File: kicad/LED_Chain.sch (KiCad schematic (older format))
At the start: 30 parts, among them J1 Interface, J2 PWR, J3 NeoPixel R1 A, J4 NeoPixel R1 B, J5 NeoPixel R1 C, J6 NeoPixel R1 D, J7 LED, Q1 IRLML2502, Q2 IRLML2502, Q3 IRLML2502, Q4 IRLML2502, U1 HCF4027B, U2 74LS04

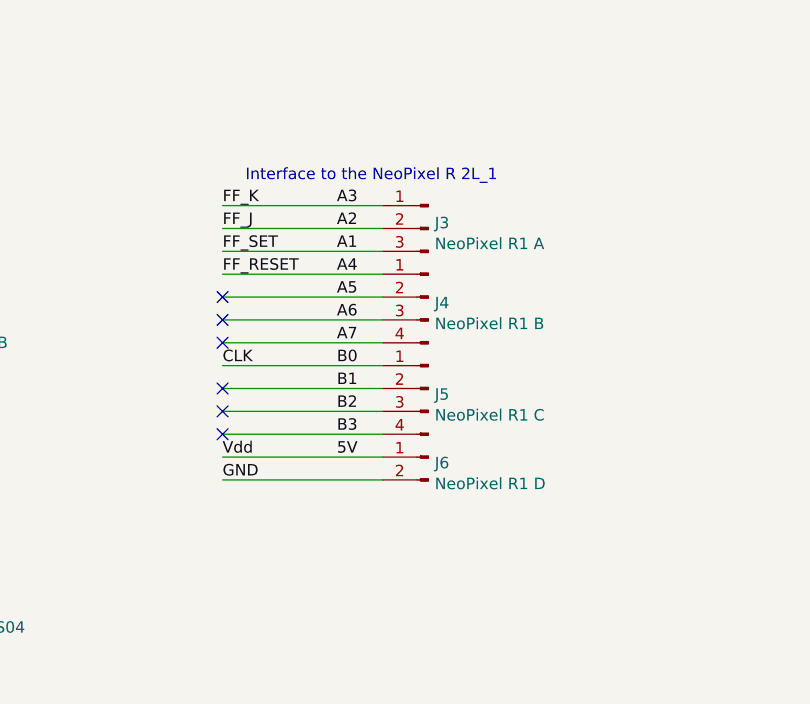
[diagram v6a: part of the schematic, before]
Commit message: Fixes the pin association on J3
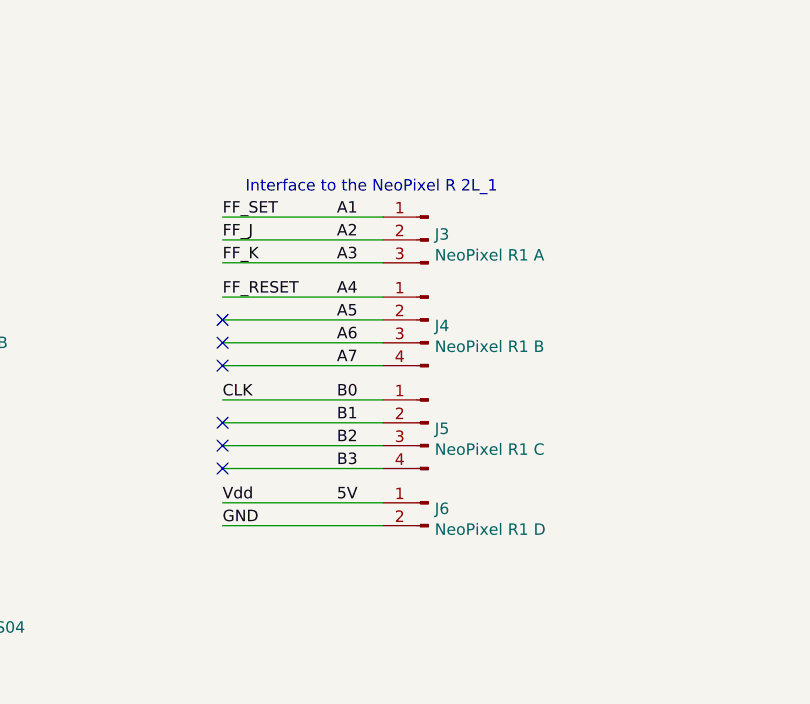
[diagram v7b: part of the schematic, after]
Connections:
- net A1: now also J3.1 (Pin_1); no longer J3.3 (Pin_3)
- net A3: now also J3.3 (Pin_3); no longer J3.1 (Pin_1)
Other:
- moved on the sheet: J3, J4, J5, J6
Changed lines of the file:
@@
 L Connector:Conn_01x04_Male J5
 U 1 1 5FA85238
-P 7750 5050
-F 0 "J5" H 7722 5024 50  0000 R CNN
-F 1 "NeoPixel R1 C" H 7722 4933 50  0000 R CNN
-F 2 "Pin_Headers:Pin_Header_Straight_1x04_Pitch2.54mm" H 7750 5050 50  0001 C CNN
-F 3 "~" H 7750 5050 50  0001 C CNN
-	1    7750 5050
+P 7750 5200
+F 0 "J5" H 7722 5174 50  0000 R CNN
+F 1 "NeoPixel R1 C" H 7722 5083 50  0000 R CNN
+F 2 "Pin_Headers:Pin_Header_Straight_1x04_Pitch2.54mm" H 7750 5200 50  0001 C CNN
+F 3 "~" H 7750 5200 50  0001 C CNN
+	1    7750 5200
 	-1   0    0    -1
 $EndComp
@@
 L Connector:Conn_01x04_Male J4
 U 1 1 5FA870C1
-P 7750 4650
-F 0 "J4" H 7722 4624 50  0000 R CNN
-F 1 "NeoPixel R1 B" H 7722 4533 50  0000 R CNN
-F 2 "Pin_Headers:Pin_Header_Straight_1x04_Pitch2.54mm" H 7750 4650 50  0001 C CNN
-F 3 "~" H 7750 4650 50  0001 C CNN
-	1    7750 4650
+P 7750 4750
+F 0 "J4" H 7722 4724 50  0000 R CNN
+F 1 "NeoPixel R1 B" H 7722 4633 50  0000 R CNN
+F 2 "Pin_Headers:Pin_Header_Straight_1x04_Pitch2.54mm" H 7750 4750 50  0001 C CNN
+F 3 "~" H 7750 4750 50  0001 C CNN
+	1    7750 4750
 	-1   0    0    -1
 $EndComp
@@
 L Connector:Conn_01x03_Male J3
 U 1 1 5FA916E0
-P 7750 4350
-F 0 "J3" H 7722 4374 50  0000 R CNN
-F 1 "NeoPixel R1 A" H 7722 4283 50  0000 R CNN
-F 2 "Pin_Headers:Pin_Header_Straight_1x03_Pitch2.54mm" H 7750 4350 50  0001 C CNN
-F 3 "~" H 7750 4350 50  0001 C CNN
-	1    7750 4350
+P 7750 4400
+F 0 "J3" H 7722 4424 50  0000 R CNN
+F 1 "NeoPixel R1 A" H 7722 4333 50  0000 R CNN
+F 2 "Pin_Headers:Pin_Header_Straight_1x03_Pitch2.54mm" H 7750 4400 50  0001 C CNN
+F 3 "~" H 7750 4400 50  0001 C CNN
+	1    7750 4400
 	-1   0    0    -1
 $EndComp
-Wire Wire Line
-	7550 4550 6850 4550
 Wire Wire Line
 	7550 4650 6850 4650
@@
 	7550 4950 6850 4950
 Wire Wire Line
-	7550 5050 6850 5050
+	7550 5100 6850 5100
 Wire Wire Line
-	7550 5250 6850 5250
+	7550 5200 6850 5200
 Wire Wire Line
-	7550 4250 6850 4250
+	7550 5400 6850 5400
 Wire Wire Line
-	7550 4350 6850 4350
+	7550 4300 6850 4300
 Wire Wire Line
-	7550 4450 6850 4450
-Text Label 7350 4550 0    50   ~ 0
+	7550 4400 6850 4400
+Wire Wire Line
+	7550 4500 6850 4500
+Text Label 7350 4650 0    50   ~ 0
 A4
-Text Label 7350 4650 0    50   ~ 0
+Text Label 7350 4750 0    50   ~ 0
 A5
-Text Label 7350 4750 0    50   ~ 0
+Text Label 7350 4850 0    50   ~ 0
 A6
-Text Label 7350 4850 0    50   ~ 0
+Text Label 7350 4950 0    50   ~ 0
 A7
-Text Label 7350 5250 0    50   ~ 0
+Text Label 7350 5400 0    50   ~ 0
 B3
-Text Label 7350 5150 0    50   ~ 0
+Text Label 7350 5300 0    50   ~ 0
 B2
-Text Label 7350 5050 0    50   ~ 0
+Text Label 7350 5200 0    50   ~ 0
 B1
-Text Label 7350 4950 0    50   ~ 0
+Text Label 7350 5100 0    50   ~ 0
 B0
-Text Label 7350 4250 0    50   ~ 0
+Text Label 7350 4500 0    50   ~ 0
 A3
-Text Label 7350 4350 0    50   ~ 0
+Text Label 7350 4400 0    50   ~ 0
 A2
-Text Label 7350 4450 0    50   ~ 0
+Text Label 7350 4300 0    50   ~ 0
 A1
 Wire Wire Line
@@
 	3450 5650 3200 5650
 Wire Wire Line
-	7550 5350 6850 5350
+	7550 5550 6850 5550
 Wire Wire Line
-	7550 5450 6850 5450
-Text Label 7350 5350 0    50   ~ 0
+	7550 5650 6850 5650
+Text Label 7350 5550 0    50   ~ 0
 5V
-Text Label 6850 5450 0    50   ~ 0
+Text Label 6850 5650 0    50   ~ 0
 GND
 $Comp
 L Connector:Conn_01x02_Male J6
 U 1 1 5FAE3734
-P 7750 5350
-F 0 "J6" H 7722 5324 50  0000 R CNN
-F 1 "NeoPixel R1 D" H 7722 5233 50  0000 R CNN
-F 2 "Pin_Headers:Pin_Header_Straight_1x02_Pitch2.54mm" H 7750 5350 50  0001 C CNN
-F 3 "~" H 7750 5350 50  0001 C CNN
-	1    7750 5350
+P 7750 5550
+F 0 "J6" H 7722 5524 50  0000 R CNN
+F 1 "NeoPixel R1 D" H 7722 5433 50  0000 R CNN
+F 2 "Pin_Headers:Pin_Header_Straight_1x02_Pitch2.54mm" H 7750 5550 50  0001 C CNN
+F 3 "~" H 7750 5550 50  0001 C CNN
+	1    7750 5550
 	-1   0    0    -1
 $EndComp
@@
 	-1   0    0    -1
 $EndComp
-Text Notes 6950 4150 0    50   ~ 0
+Text Notes 6950 4200 0    50   ~ 0
 Interface to the NeoPixel R 2L_1
 Text Notes 2900 5850 0    50   ~ 0
 Jumper for common Vbb and Vdd
 Wire Wire Line
-	7550 5150 6850 5150
-Text Label 6850 4950 0    50   ~ 0
+	7550 5300 6850 5300
+Text Label 6850 5100 0    50   ~ 0
 CLK
-Text Label 6850 4350 0    50   ~ 0
+Text Label 6850 4400 0    50   ~ 0
 FF_J
-Text Label 6850 4250 0    50   ~ 0
+Text Label 6850 4500 0    50   ~ 0
 FF_K
-Text Label 6850 4450 0    50   ~ 0
+Text Label 6850 4300 0    50   ~ 0
 FF_SET
-Text Label 6850 4550 0    50   ~ 0
+Text Label 6850 4650 0    50   ~ 0
 FF_RESET
-Text Label 6850 5350 0    50   ~ 0
+Text Label 6850 5550 0    50   ~ 0
 Vdd
-NoConn ~ 6850 4650
 NoConn ~ 6850 4750
 NoConn ~ 6850 4850
-NoConn ~ 6850 5250
-NoConn ~ 6850 5050
-NoConn ~ 6850 5150
+NoConn ~ 6850 4950
+NoConn ~ 6850 5400
+NoConn ~ 6850 5200
+NoConn ~ 6850 5300
 Wire Wire Line
 	2750 4450 3000 4450

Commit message: Revert "Fixes the pin association on J3"
This reverts commit 2cc36517f423e818af2cf15adf9433c164440afc.
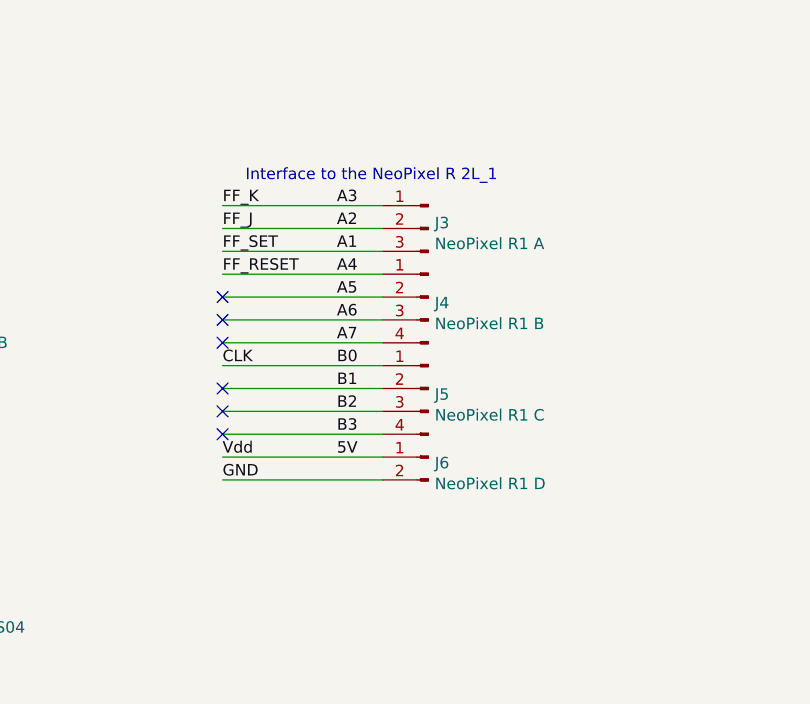
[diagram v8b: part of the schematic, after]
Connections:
- net A1: now also J3.3 (Pin_3); no longer J3.1 (Pin_1)
- net A3: now also J3.1 (Pin_1); no longer J3.3 (Pin_3)
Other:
- moved on the sheet: J3, J4, J5, J6
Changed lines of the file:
@@
 L Connector:Conn_01x04_Male J5
 U 1 1 5FA85238
-P 7750 5200
-F 0 "J5" H 7722 5174 50  0000 R CNN
-F 1 "NeoPixel R1 C" H 7722 5083 50  0000 R CNN
-F 2 "Pin_Headers:Pin_Header_Straight_1x04_Pitch2.54mm" H 7750 5200 50  0001 C CNN
-F 3 "~" H 7750 5200 50  0001 C CNN
-	1    7750 5200
+P 7750 5050
+F 0 "J5" H 7722 5024 50  0000 R CNN
+F 1 "NeoPixel R1 C" H 7722 4933 50  0000 R CNN
+F 2 "Pin_Headers:Pin_Header_Straight_1x04_Pitch2.54mm" H 7750 5050 50  0001 C CNN
+F 3 "~" H 7750 5050 50  0001 C CNN
+	1    7750 5050
 	-1   0    0    -1
 $EndComp
@@
 L Connector:Conn_01x04_Male J4
 U 1 1 5FA870C1
-P 7750 4750
-F 0 "J4" H 7722 4724 50  0000 R CNN
-F 1 "NeoPixel R1 B" H 7722 4633 50  0000 R CNN
-F 2 "Pin_Headers:Pin_Header_Straight_1x04_Pitch2.54mm" H 7750 4750 50  0001 C CNN
-F 3 "~" H 7750 4750 50  0001 C CNN
-	1    7750 4750
+P 7750 4650
+F 0 "J4" H 7722 4624 50  0000 R CNN
+F 1 "NeoPixel R1 B" H 7722 4533 50  0000 R CNN
+F 2 "Pin_Headers:Pin_Header_Straight_1x04_Pitch2.54mm" H 7750 4650 50  0001 C CNN
+F 3 "~" H 7750 4650 50  0001 C CNN
+	1    7750 4650
 	-1   0    0    -1
 $EndComp
@@
 L Connector:Conn_01x03_Male J3
 U 1 1 5FA916E0
-P 7750 4400
-F 0 "J3" H 7722 4424 50  0000 R CNN
-F 1 "NeoPixel R1 A" H 7722 4333 50  0000 R CNN
-F 2 "Pin_Headers:Pin_Header_Straight_1x03_Pitch2.54mm" H 7750 4400 50  0001 C CNN
-F 3 "~" H 7750 4400 50  0001 C CNN
-	1    7750 4400
+P 7750 4350
+F 0 "J3" H 7722 4374 50  0000 R CNN
+F 1 "NeoPixel R1 A" H 7722 4283 50  0000 R CNN
+F 2 "Pin_Headers:Pin_Header_Straight_1x03_Pitch2.54mm" H 7750 4350 50  0001 C CNN
+F 3 "~" H 7750 4350 50  0001 C CNN
+	1    7750 4350
 	-1   0    0    -1
 $EndComp
+Wire Wire Line
+	7550 4550 6850 4550
 Wire Wire Line
 	7550 4650 6850 4650
@@
 	7550 4950 6850 4950
 Wire Wire Line
-	7550 5100 6850 5100
+	7550 5050 6850 5050
 Wire Wire Line
-	7550 5200 6850 5200
+	7550 5250 6850 5250
 Wire Wire Line
-	7550 5400 6850 5400
+	7550 4250 6850 4250
 Wire Wire Line
-	7550 4300 6850 4300
+	7550 4350 6850 4350
 Wire Wire Line
-	7550 4400 6850 4400
-Wire Wire Line
-	7550 4500 6850 4500
+	7550 4450 6850 4450
+Text Label 7350 4550 0    50   ~ 0
+A4
 Text Label 7350 4650 0    50   ~ 0
-A4
+A5
 Text Label 7350 4750 0    50   ~ 0
-A5
+A6
 Text Label 7350 4850 0    50   ~ 0
-A6
+A7
+Text Label 7350 5250 0    50   ~ 0
+B3
+Text Label 7350 5150 0    50   ~ 0
+B2
+Text Label 7350 5050 0    50   ~ 0
+B1
 Text Label 7350 4950 0    50   ~ 0
-A7
-Text Label 7350 5400 0    50   ~ 0
-B3
-Text Label 7350 5300 0    50   ~ 0
-B2
-Text Label 7350 5200 0    50   ~ 0
-B1
-Text Label 7350 5100 0    50   ~ 0
 B0
-Text Label 7350 4500 0    50   ~ 0
+Text Label 7350 4250 0    50   ~ 0
 A3
-Text Label 7350 4400 0    50   ~ 0
+Text Label 7350 4350 0    50   ~ 0
 A2
-Text Label 7350 4300 0    50   ~ 0
+Text Label 7350 4450 0    50   ~ 0
 A1
 Wire Wire Line
@@
 	3450 5650 3200 5650
 Wire Wire Line
-	7550 5550 6850 5550
+	7550 5350 6850 5350
 Wire Wire Line
-	7550 5650 6850 5650
-Text Label 7350 5550 0    50   ~ 0
+	7550 5450 6850 5450
+Text Label 7350 5350 0    50   ~ 0
 5V
-Text Label 6850 5650 0    50   ~ 0
+Text Label 6850 5450 0    50   ~ 0
 GND
 $Comp
 L Connector:Conn_01x02_Male J6
 U 1 1 5FAE3734
-P 7750 5550
-F 0 "J6" H 7722 5524 50  0000 R CNN
-F 1 "NeoPixel R1 D" H 7722 5433 50  0000 R CNN
-F 2 "Pin_Headers:Pin_Header_Straight_1x02_Pitch2.54mm" H 7750 5550 50  0001 C CNN
-F 3 "~" H 7750 5550 50  0001 C CNN
-	1    7750 5550
+P 7750 5350
+F 0 "J6" H 7722 5324 50  0000 R CNN
+F 1 "NeoPixel R1 D" H 7722 5233 50  0000 R CNN
+F 2 "Pin_Headers:Pin_Header_Straight_1x02_Pitch2.54mm" H 7750 5350 50  0001 C CNN
+F 3 "~" H 7750 5350 50  0001 C CNN
+	1    7750 5350
 	-1   0    0    -1
 $EndComp
@@
 	-1   0    0    -1
 $EndComp
-Text Notes 6950 4200 0    50   ~ 0
+Text Notes 6950 4150 0    50   ~ 0
 Interface to the NeoPixel R 2L_1
 Text Notes 2900 5850 0    50   ~ 0
 Jumper for common Vbb and Vdd
 Wire Wire Line
-	7550 5300 6850 5300
-Text Label 6850 5100 0    50   ~ 0
+	7550 5150 6850 5150
+Text Label 6850 4950 0    50   ~ 0
 CLK
-Text Label 6850 4400 0    50   ~ 0
+Text Label 6850 4350 0    50   ~ 0
 FF_J
-Text Label 6850 4500 0    50   ~ 0
+Text Label 6850 4250 0    50   ~ 0
 FF_K
-Text Label 6850 4300 0    50   ~ 0
+Text Label 6850 4450 0    50   ~ 0
 FF_SET
-Text Label 6850 4650 0    50   ~ 0
+Text Label 6850 4550 0    50   ~ 0
 FF_RESET
-Text Label 6850 5550 0    50   ~ 0
+Text Label 6850 5350 0    50   ~ 0
 Vdd
+NoConn ~ 6850 4650
 NoConn ~ 6850 4750
 NoConn ~ 6850 4850
-NoConn ~ 6850 4950
-NoConn ~ 6850 5400
-NoConn ~ 6850 5200
-NoConn ~ 6850 5300
+NoConn ~ 6850 5250
+NoConn ~ 6850 5050
+NoConn ~ 6850 5150
 Wire Wire Line
 	2750 4450 3000 4450
